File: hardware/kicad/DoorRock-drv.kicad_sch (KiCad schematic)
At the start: 7 parts, among them J2 Conn_01x04_Socket, J3 Conn_01x02_Socket, Q2 IRLZ44N, SW1 SW_SPDT

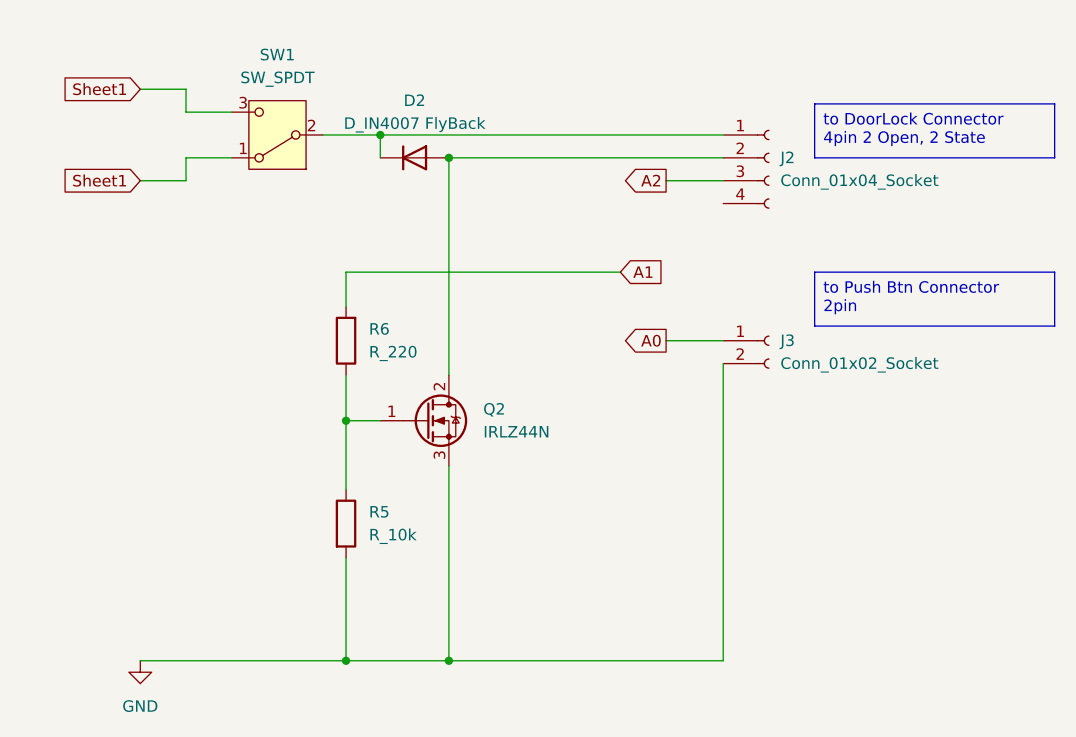
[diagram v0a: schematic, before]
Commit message: chore: KiCad 회로도 최신 변경사항 반영
원본 작업 폴더가 "회로도 편집 완료/20260901_ver01"로 재구성됨(이전 smartvault-pcb-1
경로는 더 이상 존재하지 않음). 하위 시트 6개 전부와 최상위 시트에 실제 설계 변경
있음(DoorRock-drv는 축소, 최상위 시트는 대폭 확장 — 회로가 재구성된 것으로 보임).
PCB 레이아웃 자체는 변경 없음. footprint.xlsx(부품-풋프린트 매핑) 신규 추가.

파일 내부의 프로젝트명 자기참조는 원본 작업 파일명("20260901_ver01")이 아니라
저장소 표준 이름("smartvault")으로 맞춰서 복사 — 작업 폴더 쪽 날짜/버전 파일명
관례를 저장소까지 끌고 오지 않음(git이 버전을 관리).

s_vault.kicad_sym(커스텀 심볼 라이브러리)은 원본 경로에서 찾지 못해 갱신 못함 —
RS485-com/power 시트가 이 라이브러리를 참조하므로, 최신 심볼이 바뀌었다면 다음에
갱신 필요(hardware/README.md에 기록해둠).

Co-Authored-By: Claude Sonnet 5 <noreply@anthropic.com>
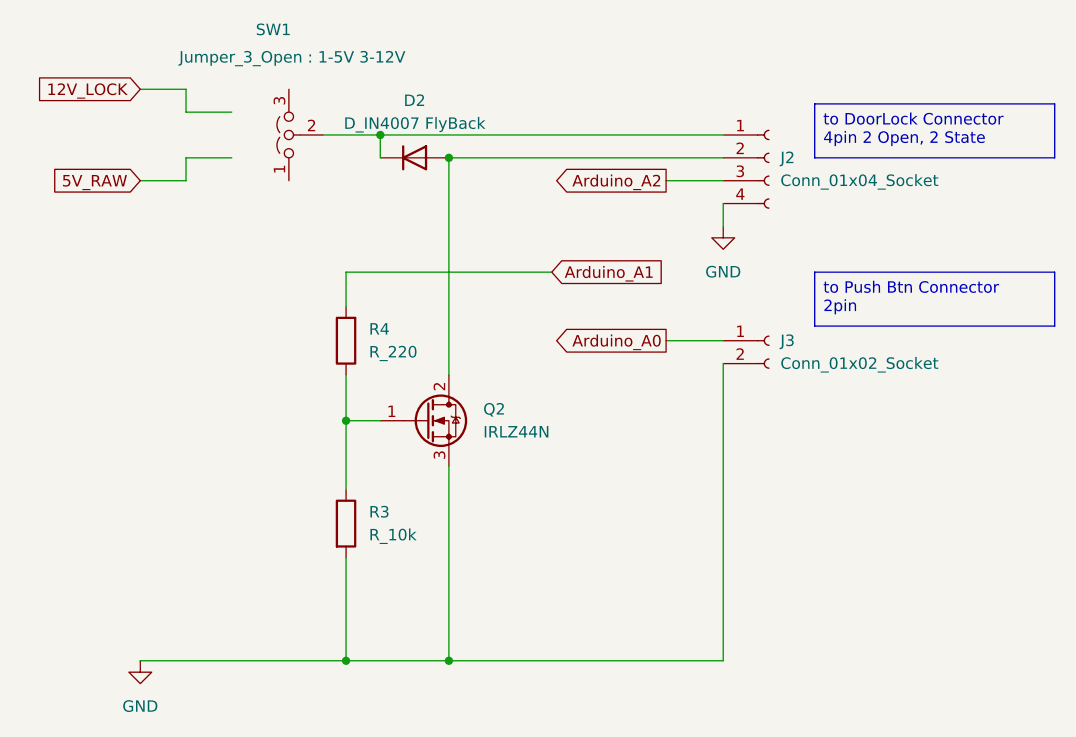
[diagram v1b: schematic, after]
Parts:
- removed SW1: SW_SPDT, symbol Switch:SW_SPDT
- added SW1: Jumper_3_Open : 1-5V 3-12V, Connector_PinHeader_2.54mm:PinHeader_1x03_P2.54mm_Vertical, symbol Jumper:Jumper_3_Open
- D2: footprint (none) -> Diode_THT:D_DO-41_SOD81_P10.16mm
- J2: footprint (none) -> Connector_JST:JST_XH_B4B-XH-A_1x04_P2.50mm_Vertical
- J3: footprint (none) -> Connector_JST:JST_XH_B2B-XH-A_1x02_P2.50mm_Vertical
- R3: renamed from R5; footprint (none) -> Resistor_SMD:R_0805_2012Metric
- R4: renamed from R6; footprint (none) -> Resistor_SMD:R_0805_2012Metric
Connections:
- net GND: now also J2.4 (Pin_4)
- net at D2.1 (K), J2.1 (Pin_1): now also SW1.2 (C)
- net A0 renamed Arduino_A0
- net A1 renamed Arduino_A1
- net A2 renamed Arduino_A2
